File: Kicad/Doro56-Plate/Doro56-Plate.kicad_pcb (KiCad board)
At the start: 2 copper layers, 175.4 x 115.2 mm, 0 parts

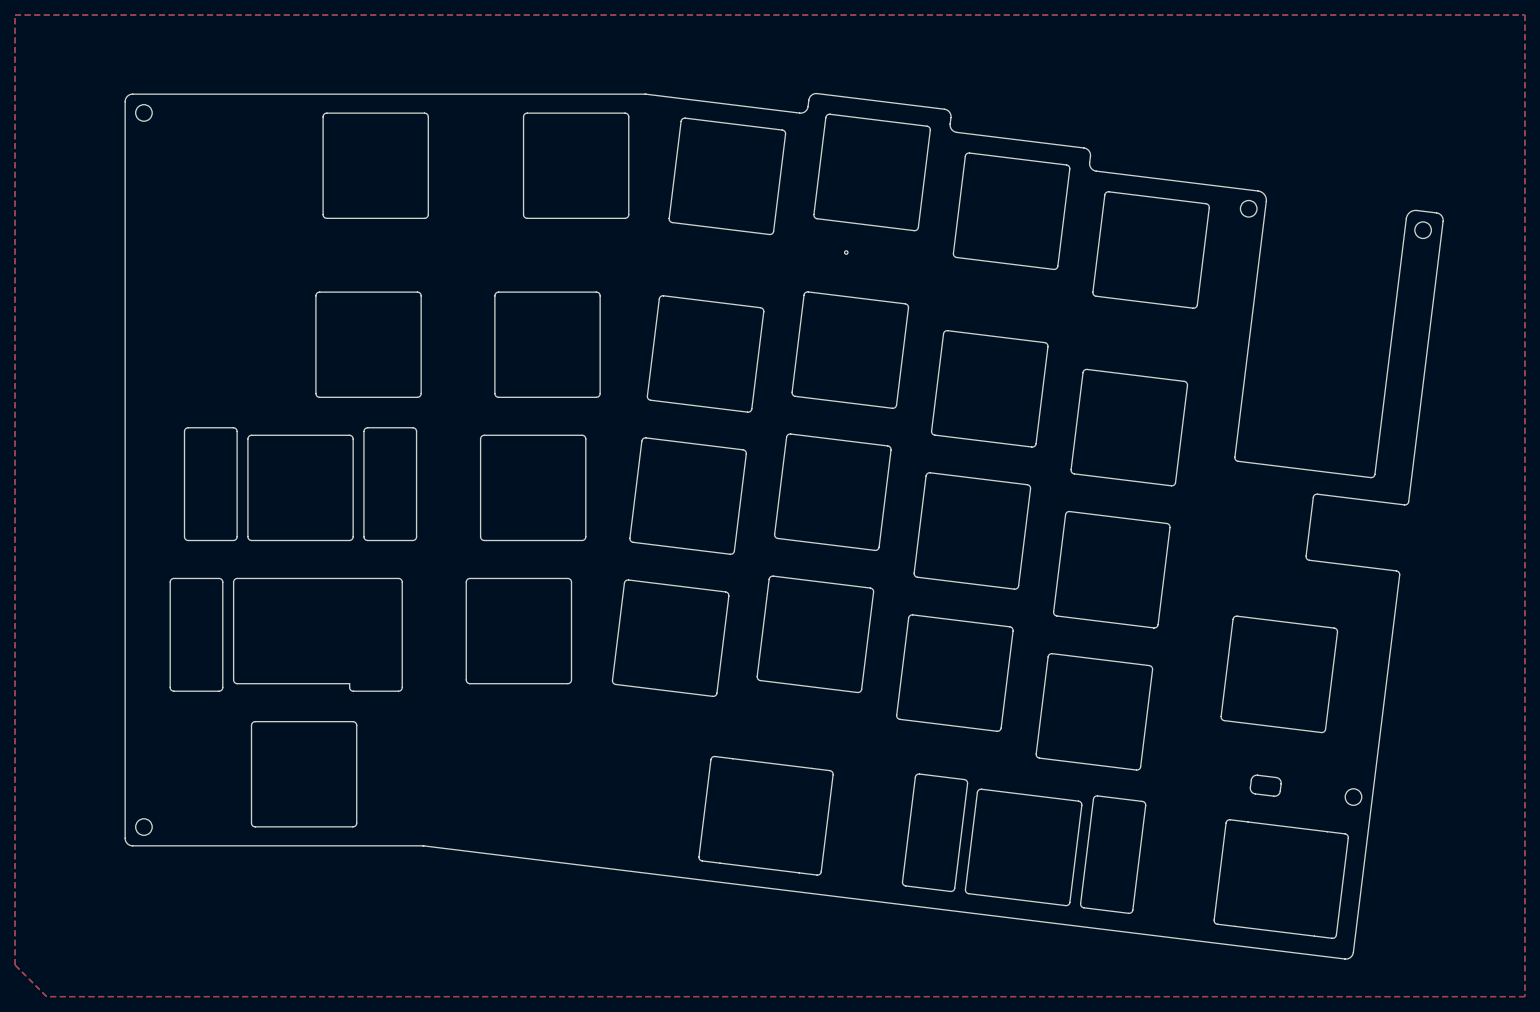
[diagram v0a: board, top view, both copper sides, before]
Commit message: v1.1
v1.1 - Minor Edit
Caps and Enter Footprints: Changed to a reversible footprint (previously used two single key footprints rotated).
JST PH Footprint: Adjusted and relocated for increased flexibility.
PCB Cutout: Modified to remove blank space between Control and Alt keys, allowing space for a 402030 battery without increasing the case height clearance.
Plate: Slightly increased the cutout size for the rotary encoder.
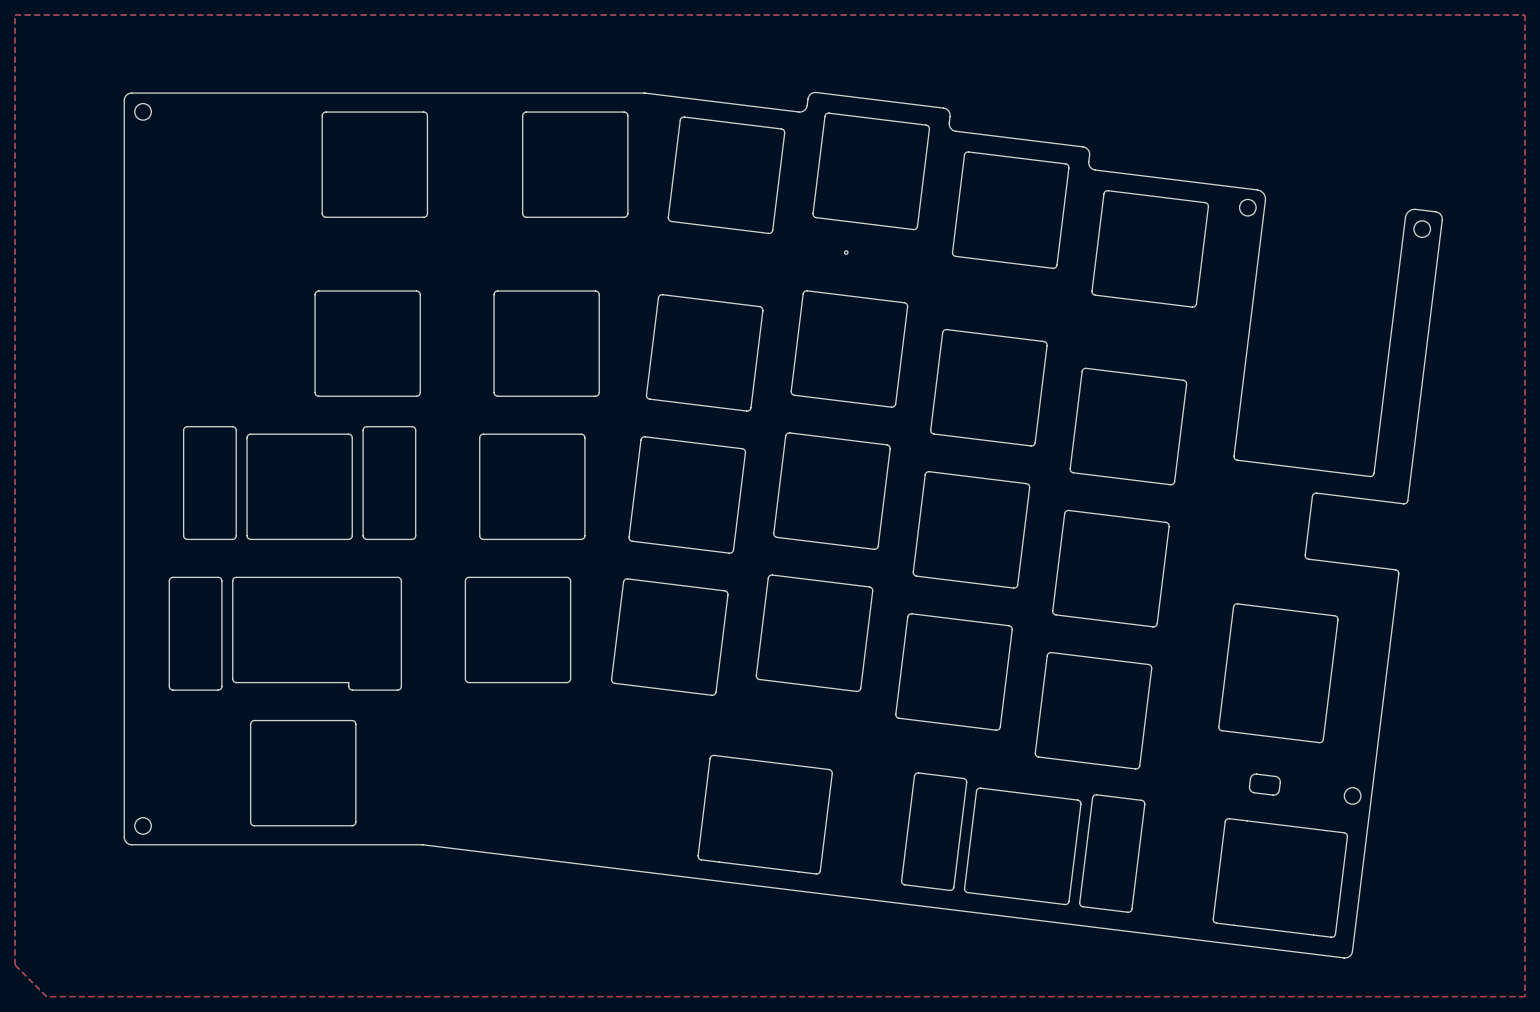
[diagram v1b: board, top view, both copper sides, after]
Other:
- outline, holes or cut-outs redrawn
